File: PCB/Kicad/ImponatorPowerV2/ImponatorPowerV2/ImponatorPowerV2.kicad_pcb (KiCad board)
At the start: 4 copper layers, 73.9 x 54.3 mm, 162 parts, among them IC1 IS31FL3728-QFLS2-TR, J1 USB type-c, J2 Conn_01x02, J3 Conn_01x04_Pin, Q1 AO3400A, Q2 AO3400A, U1 STUSB4500QTR, U10 AO3401A, U11 ACS37041, U2 EFM8UB10F16G, U3 TPS62A01DRLR, U4 ACS37041, U5 MAX4466EXK+T, U6 MCP73831T-2ACI/OT, U7 TPS62A01DRLR, U8 ACS37041

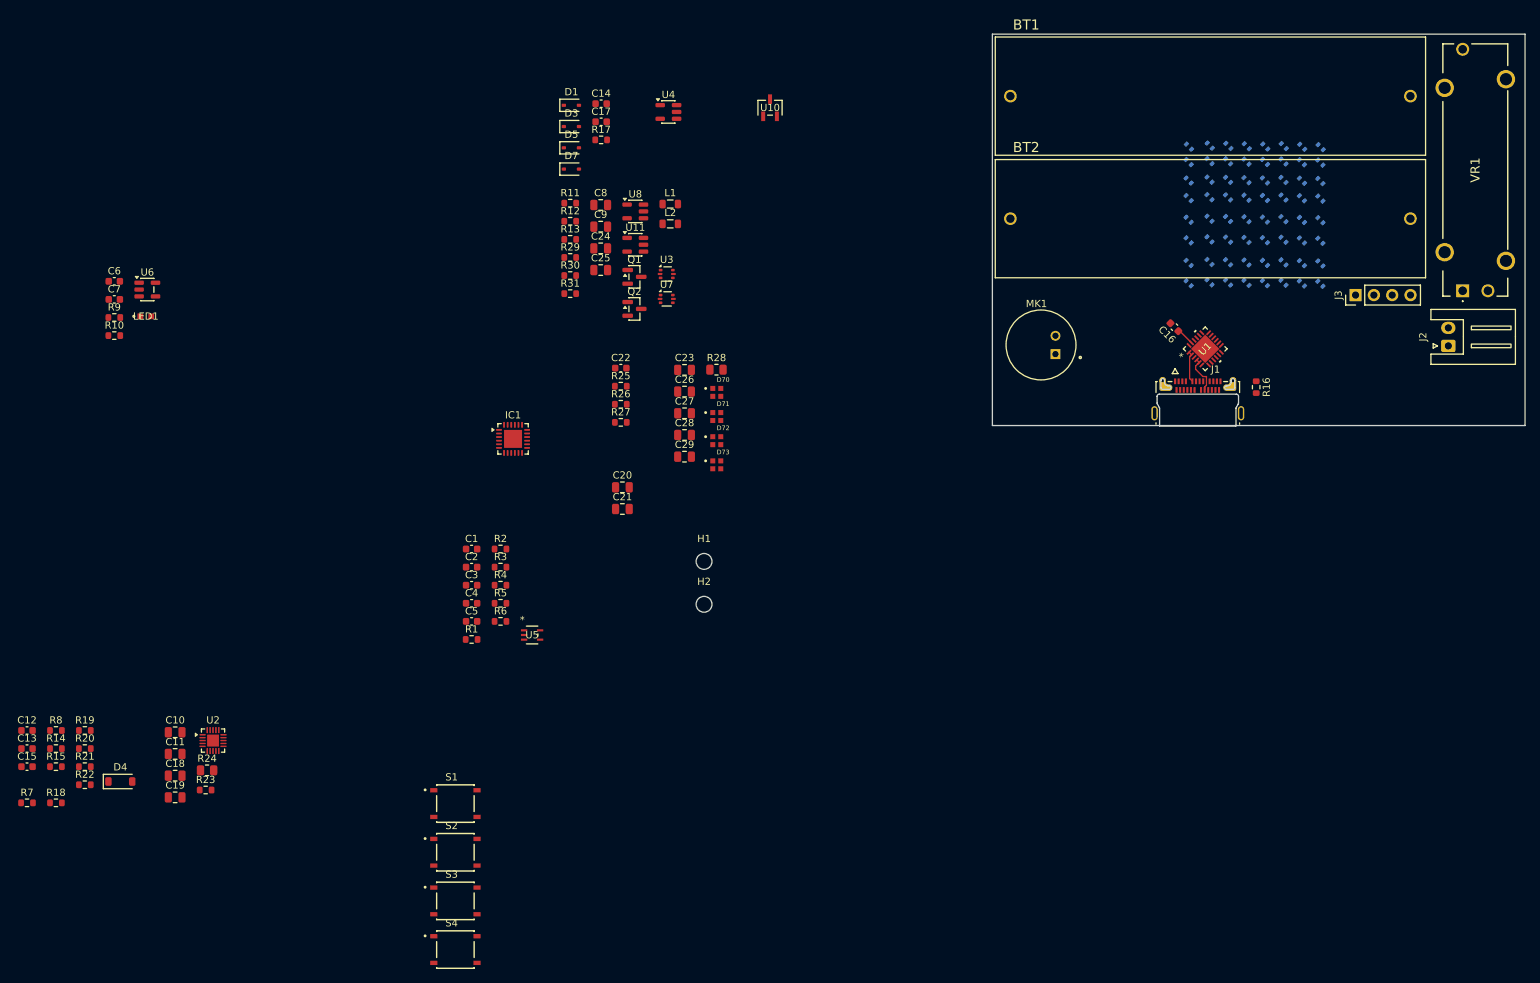
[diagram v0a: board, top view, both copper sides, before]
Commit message: PCB routed, not ready for production
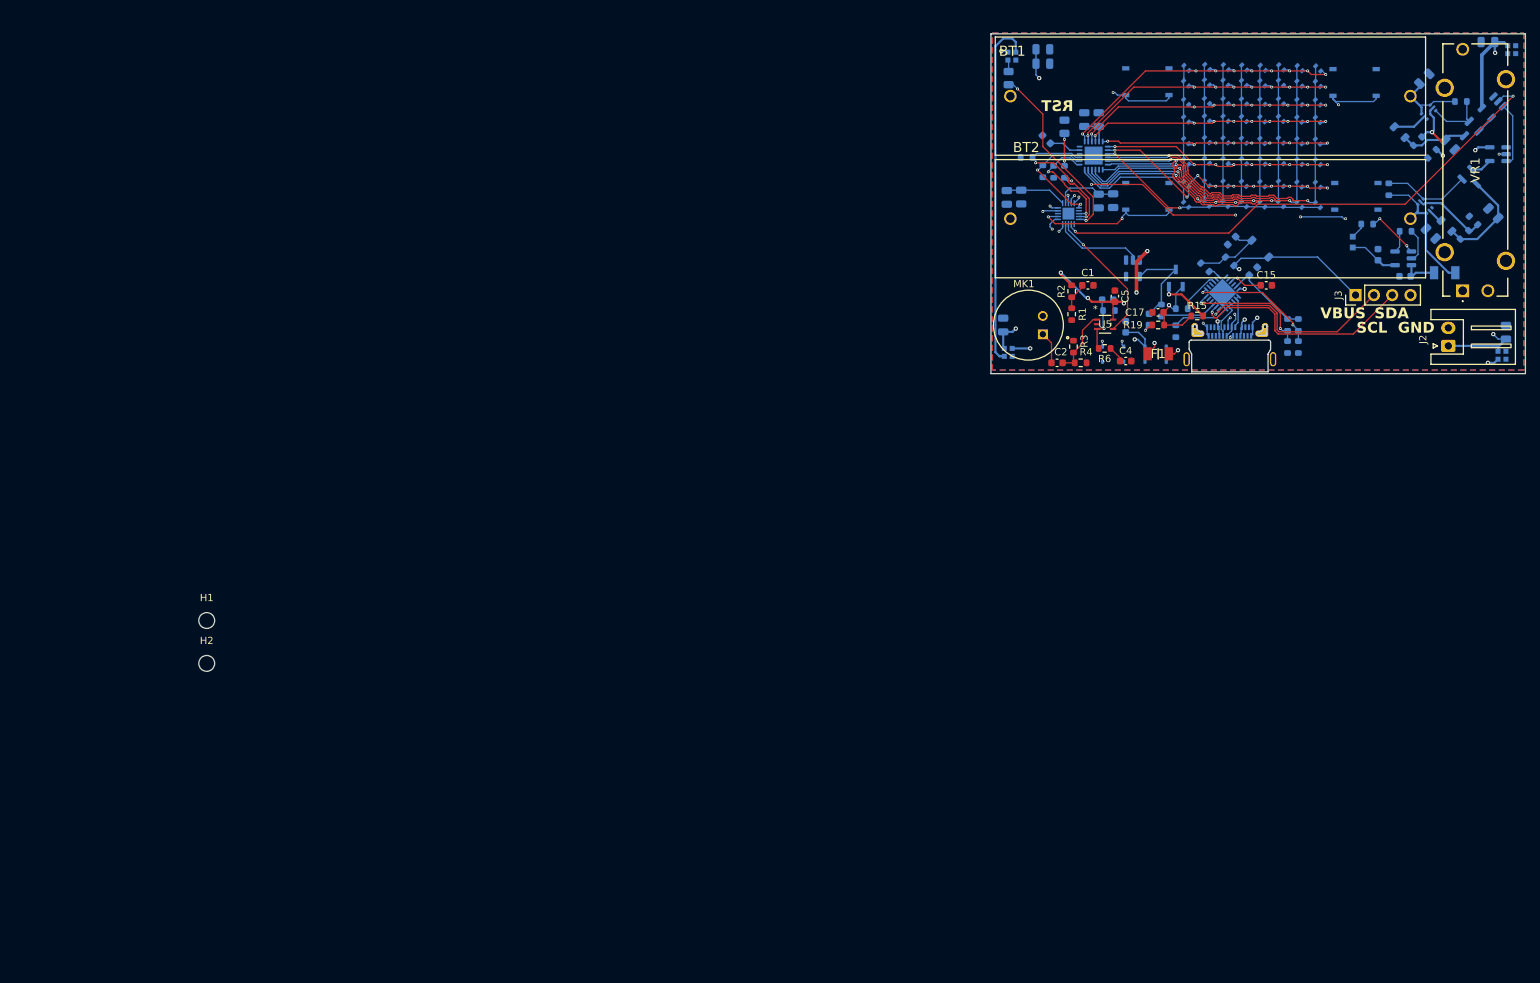
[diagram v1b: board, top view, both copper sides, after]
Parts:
- added F1: 1206L150THWR, custom2:FUSC3216X100N, F.Cu at (189.0, 82.2)
- added F2: 1206L150THWR, custom2:FUSC3216X100N, B.Cu at (228.8, 71.0)
- C10, C11, C12, C13, C14, C16, C18, C19, C20, C21, C22, C23, C24, C25, C26, C27, C28, C29, C3, C6, C7, C8, C9, D1, D3, D4, D5, D7, D70, D71, D72, D73, IC1, J1, L1, L2, LED1, Q1, Q2, R10, R11, R12, R13, R14, R16, R17, R18, R20, R21, R22, R23, R24, R25, R26, R27, R28, R29, R30, R31, R5, R7, R8, R9, S1, S2, S3, S4, U1, U10, U11, U2, U3, U4, U6, U7, U8: moved to B.Cu
- moved C15 184.4 mm to (204.0, 72.8)
- moved R7 183.0 mm to (198.9, 69.4), turned to -45 degrees
- moved R18 182.2 mm to (206.9, 81.3), turned to -90 degrees
- moved C12 180.4 mm to (199.2, 66.5), turned to 45 degrees
- moved R10 179.7 mm to (223.3, 65.2)
- moved R21 179.2 mm to (208.4, 78.2), turned to -90 degrees
- moved C7 179.1 mm to (223.2, 71.5)
- moved R22 179.0 mm to (208.4, 81.3), turned to -90 degrees
- moved R20 176.9 mm to (206.9, 78.2), turned to -90 degrees
- moved C6 175.4 mm to (219.5, 68.5), turned to -90 degrees
- moved D4 174.6 mm to (203.2, 67.7), turned to -45 degrees
- moved R9 174.3 mm to (218.0, 64.2)
- moved U6 174.3 mm to (223.0, 69.0), turned to 180 degrees
- moved R8 171.9 mm to (195.5, 70.2), turned to 135 degrees
- moved R15 170.2 mm to (194.4, 77.0)
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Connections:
- C3 pad 1: +3V3Bat -> /Microcontroller/Mic_sig
- C7 pad 2: V_bat -> /Battery and charging/VBAT
- D33 pad 2: unconnected-(D33-A-Pad2) -> /Microcontroller/LED matrix/R1
- J1 pad A4: /USB/VBUS -> Net-(J1-VBUS1)
- J1 pad A9: /USB/VBUS -> Net-(J1-VBUS1)
- J1 pad B4: /USB/VBUS -> Net-(J1-VBUS1)
- J1 pad B9: /USB/VBUS -> Net-(J1-VBUS1)
- L2 pad 1: /Battery and charging/Battery Bucks/SW -> /Battery and charging/Battery Bucks/SW2
- Q2 pad 2: /Battery and charging/Battery Bucks/PG -> /Battery and charging/Battery Bucks/PG2
- R22 pad 1: +2V7 -> Net-(U1-ADDR1)
- R29 pad 2: /Battery and charging/Battery Bucks/PG -> /Battery and charging/Battery Bucks/PG2
- R3 pad 2: +3.3V -> +3V3Bat
- R5 pad 2: +3V3Bat -> /Microcontroller/Mic_sig
- U11 pad 5: 5VBat_current -> 3VBat_current
- U2 pad 10: unconnected-(U2-P2.0-Pad10) -> 3VBat_current
- U2 pad 18: +3V3Bat -> /Microcontroller/Mic_sig
- U5 pad 4: +3V3Bat -> /Microcontroller/Mic_sig
- U6 pad 3: V_bat -> /Battery and charging/VBAT
- U7 pad 2: /Battery and charging/Battery Bucks/SW -> /Battery and charging/Battery Bucks/SW2
- U7 pad 6: /Battery and charging/Battery Bucks/PG -> /Battery and charging/Battery Bucks/PG2
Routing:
- net +5VBat: track 0.00 -> 193.7 mm, vias 0 -> 5
- net +3V3Bat: track 0.00 -> 96.4 mm, vias 0 -> 6
- net Net-(D71-DOUT): track 0.00 -> 79.8 mm, vias 0 -> 2
- net /Microcontroller/Slider: track 0.00 -> 72.9 mm, vias 0 -> 1
- net 5VBat_current: track 0.00 -> 72.3 mm, vias 0 -> 2
- net /USB/VBUS: track 0.00 -> 70.1 mm, vias 0 -> 5
- net 3VBat_current: track 0.00 -> 68.6 mm, vias 0 -> 6
- net /Microcontroller/Next_btn: track 0.00 -> 65.4 mm, vias 0 -> 2
- net /Microcontroller/LED matrix/C8: track 0.00 -> 52.2 mm, vias 0 -> 2
- net D-: track 0.00 -> 51.2 mm, vias 0 -> 4
- net /Microcontroller/LED matrix/C7: track 0.00 -> 49.4 mm, vias 0 -> 2
- net V_bat: track 0.00 -> 49.2 mm
- net D+: track 0.00 -> 48.9 mm, vias 0 -> 3
- net Net-(D70-DOUT): track 0.00 -> 48.8 mm
- net /Microcontroller/LED matrix/C6: track 0.00 -> 48.6 mm, vias 0 -> 2
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- added copper zone on B.Cu, net GND
- added copper zone on F.Cu, net GND
- added copper zone on In1.Cu, net GND
- added copper zone on In2.Cu, net GND
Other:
- board size 73.9 x 54.3 mm -> 74.1 x 47.1 mm
- board text added: "GND"
- board text added: "RST"
- board text added: "SCL"
- board text added: "SDA"
- board text added: "VBUS"
